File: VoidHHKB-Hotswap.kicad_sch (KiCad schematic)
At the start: 28 parts, among them J1 SM04B-SRSS-TB, J2 TC2030_SWD, U1 XC6206P332MR, U2 STM32F072CBT6

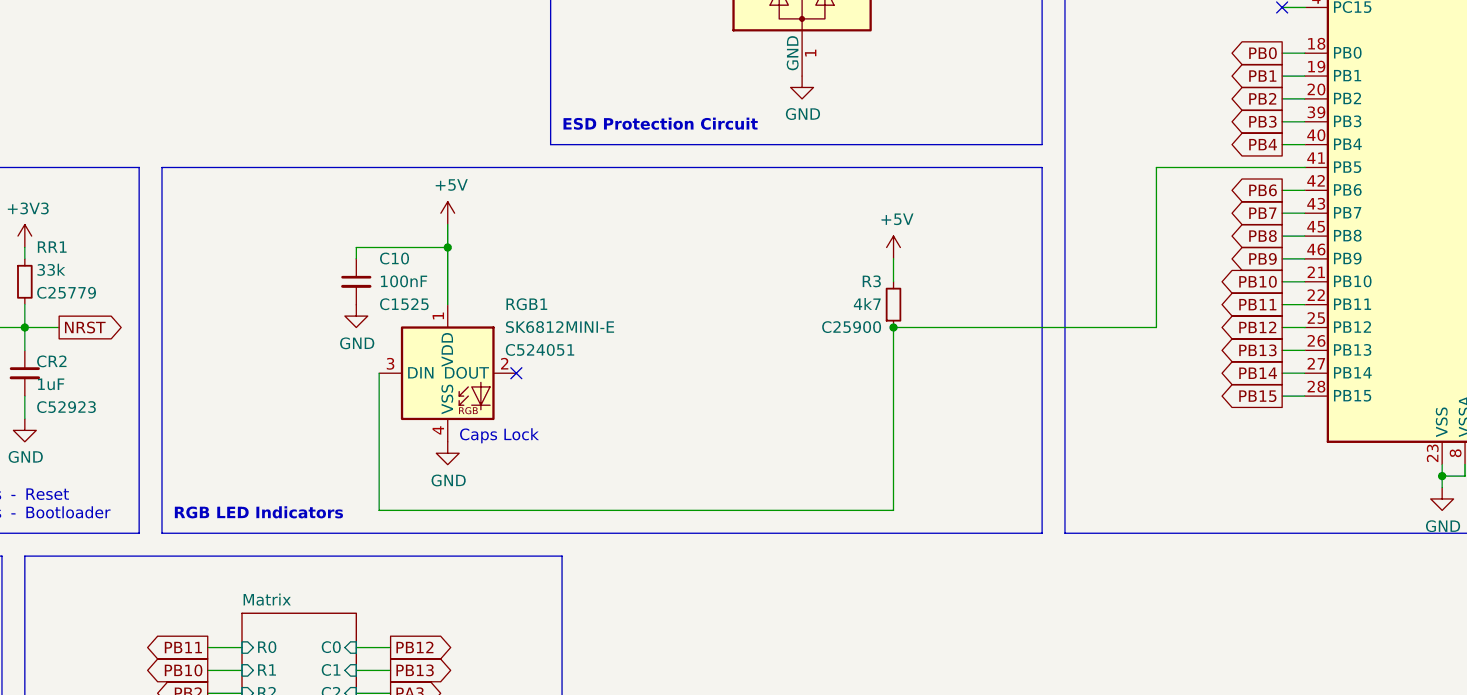
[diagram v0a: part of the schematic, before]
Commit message: Removed switch sockets that can't be used due to plate limitations.
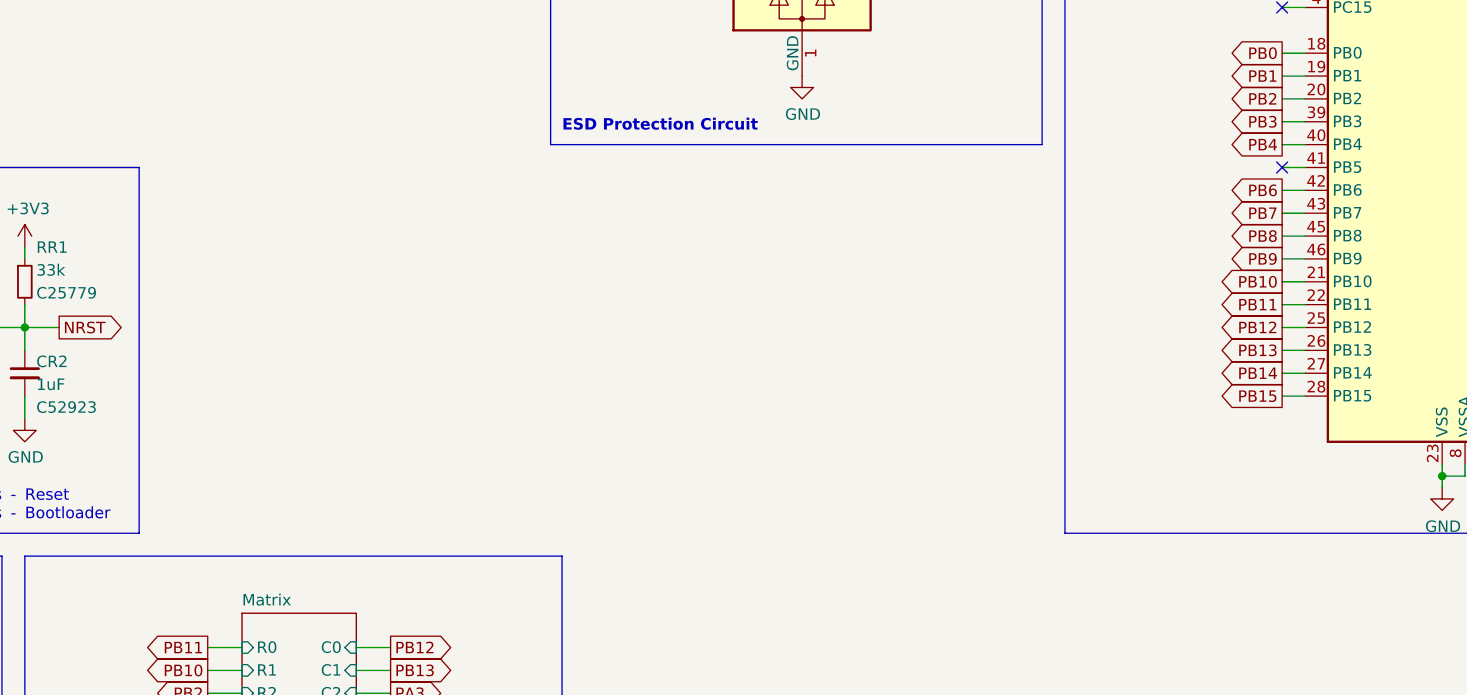
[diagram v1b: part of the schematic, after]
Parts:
- removed C10: 100nF, Capacitor_SMD:C_0402_1005Metric, symbol Device:C_Small
- removed R3: 4k7, Resistor_SMD:R_0402_1005Metric, symbol Device:R_Small
- removed RGB1: SK6812MINI-E, PCM_marbastlib-various:LED_6028R, symbol PCM_marbastlib-various:SK6812MINI-E
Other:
- note removed: "Caps Lock"
- note removed: "RGB LED Indicators"
